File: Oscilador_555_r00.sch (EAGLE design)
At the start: 8 parts, among them IC1 LM555

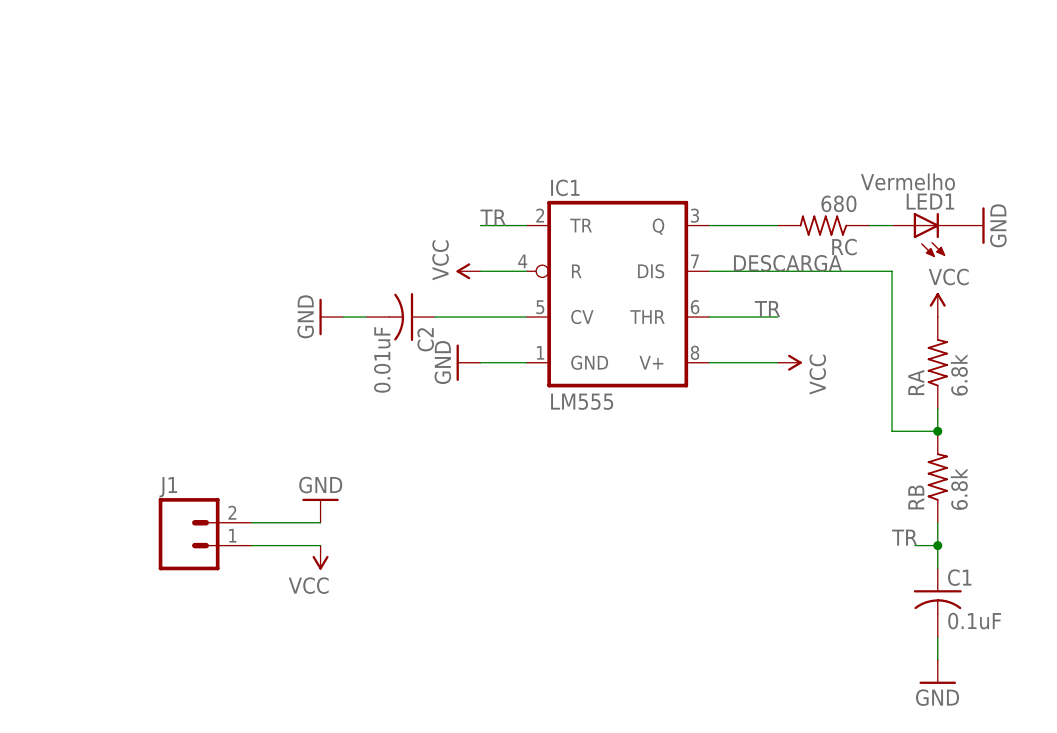
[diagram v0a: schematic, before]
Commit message: Primeira revisao e arquivos zip para producao
Primeira revisão (estética e para adicionar conector KRE 5mm); criado
Gerber para producao da PCI
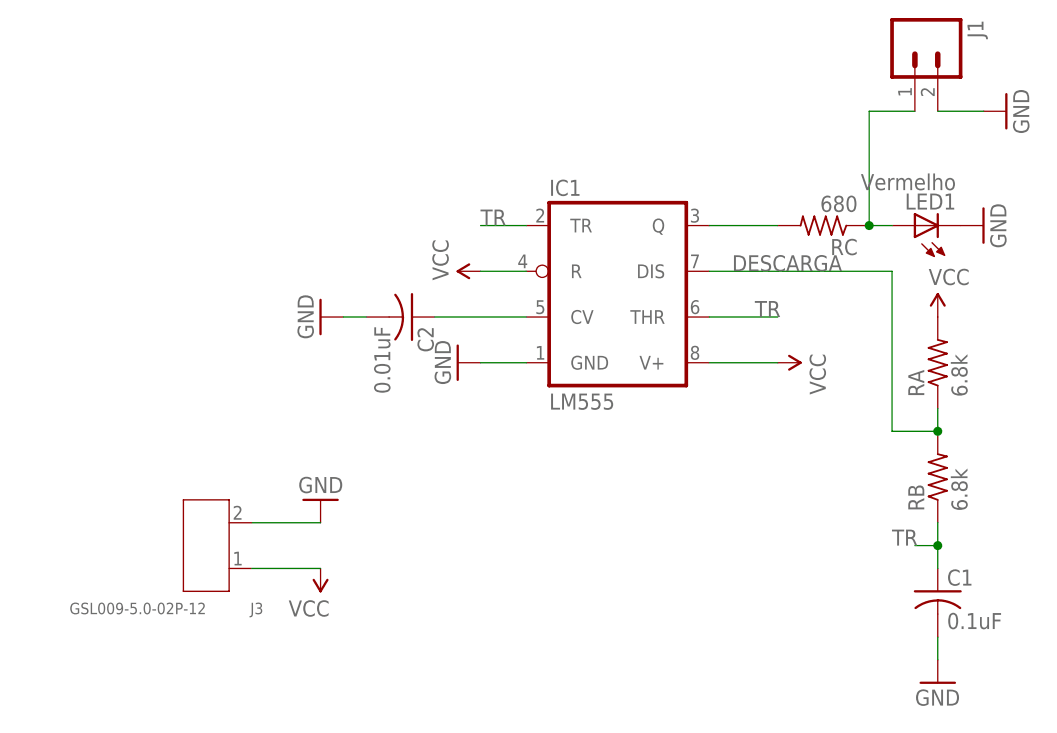
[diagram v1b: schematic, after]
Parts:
- added J3: GSL009-5.0-02P-12, Seeed-OPL-Connector:SCREW-TERMINAL-BLUE(2P-5.0)
- J1: device SparkFun-Connectors:M02POLAR -> SparkFun-Connectors:M02PTH
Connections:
- net GND: now also J3.2
- net N$3: now also J1.1
- net VCC: now also J3.1; no longer J1.1
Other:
- moved on the sheet: J1
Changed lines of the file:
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@@
 <layer number="115" name="ReferenceISLANDS" color="7" fill="1" visible="yes" active="yes"/>
 <layer number="116" name="Patch_BOT" color="9" fill="4" visible="no" active="yes"/>
+<layer number="117" name="BACKMAAT1" color="7" fill="1" visible="no" active="no"/>
 <layer number="118" name="Rect_Pads" color="7" fill="1" visible="no" active="no"/>
+<layer number="119" name="KAP_TEKEN" color="7" fill="1" visible="no" active="no"/>
+<layer number="120" name="KAP_MAAT1" color="7" fill="1" visible="no" active="no"/>
 <layer number="121" name="_tsilk" color="7" fill="1" visible="no" active="yes"/>
 <layer number="122" name="_bsilk" color="7" fill="1" visible="no" active="yes"/>
@@
 <layer number="128" name="_bValues" color="7" fill="1" visible="no" active="yes"/>
 <layer number="129" name="Mask" color="7" fill="1" visible="yes" active="yes"/>
+<layer number="130" name="SMDSTROOK" color="7" fill="1" visible="no" active="no"/>
 <layer number="131" name="tAdjust" color="7" fill="1" visible="no" active="yes"/>
 <layer number="132" name="bAdjust" color="7" fill="1" visible="no" active="yes"/>
+<layer number="133" name="bottom_silk" color="7" fill="1" visible="no" active="no"/>
 <layer number="144" name="Drill_legend" color="7" fill="1" visible="no" active="yes"/>
 <layer number="150" name="Notes" color="7" fill="1" visible="no" active="yes"/>
@@
 <part name="C1" library="adafruit" deviceset="C-US" device="050-024X044" value="0.1uF"/>
 <part name="GND4" library="SparkFun-Aesthetics" deviceset="GND" device=""/>
-<part name="J1" library="SparkFun-Connectors" deviceset="M02" device="POLAR"/>
 <part name="SUPPLY4" library="SparkFun-Aesthetics" deviceset="VCC" device=""/>
 <part name="GND5" library="SparkFun-Aesthetics" deviceset="GND" device=""/>
+<part name="J1" library="SparkFun-Connectors" deviceset="M02" device="PTH"/>
+<part name="GND6" library="SparkFun-Aesthetics" deviceset="GND" device=""/>
+<part name="J3" library="Seeed-OPL-Connector" deviceset="SCREW-TERMINAL-BLUE(2P-5.0)" device="" value="GSL009-5.0-02P-12"/>
 </parts>
 <sheets>
@@
 <instance part="C1" gate="G$1" x="93.98" y="5.08"/>
 <instance part="GND4" gate="1" x="93.98" y="-5.08"/>
-<instance part="J1" gate="G$1" x="10.16" y="10.16"/>
-<instance part="SUPPLY4" gate="G$1" x="25.4" y="10.16" rot="R180"/>
+<instance part="SUPPLY4" gate="G$1" x="25.4" y="7.62" rot="R180"/>
 <instance part="GND5" gate="1" x="25.4" y="15.24" rot="R180"/>
+<instance part="J1" gate="G$1" x="91.44" y="66.04" rot="R270"/>
+<instance part="GND6" gate="1" x="101.6" y="58.42" rot="R90"/>
+<instance part="J3" gate="G$1" x="12.7" y="10.16" rot="R180"/>
 </instances>
 <busses>
@@
 </segment>
 <segment>
-<pinref part="J1" gate="G$1" pin="1"/>
 <pinref part="SUPPLY4" gate="G$1" pin="VCC"/>
-<wire x1="25.4" y1="10.16" x2="17.78" y2="10.16" width="0.1524" layer="91"/>
+<wire x1="25.4" y1="7.62" x2="17.78" y2="7.62" width="0.1524" layer="91"/>
+<pinref part="J3" gate="G$1" pin="1"/>
 </segment>
 </net>
@@
 </segment>
 <segment>
-<pinref part="J1" gate="G$1" pin="2"/>
 <pinref part="GND5" gate="1" pin="GND"/>
 <wire x1="25.4" y1="12.7" x2="17.78" y2="12.7" width="0.1524" layer="91"/>
+<pinref part="J3" gate="G$1" pin="2"/>
+</segment>
+<segment>
+<pinref part="J1" gate="G$1" pin="2"/>
+<pinref part="GND6" gate="1" pin="GND"/>
+<wire x1="99.06" y1="58.42" x2="93.98" y2="58.42" width="0.1524" layer="91"/>
 </segment>
 </net>
@@
 <pinref part="RC" gate="G$1" pin="1"/>
 <wire x1="88.9" y1="45.72" x2="86.36" y2="45.72" width="0.1524" layer="91"/>
-</segment>
-</net>
+<pinref part="J1" gate="G$1" pin="1"/>
+<wire x1="91.44" y1="58.42" x2="86.36" y2="58.42" width="0.1524" layer="91"/>
+<wire x1="86.36" y1="58.42" x2="86.36" y2="45.72" width="0.1524" layer="91"/>
+<junction x="86.36" y="45.72"/>
+</segment>
+</net>
